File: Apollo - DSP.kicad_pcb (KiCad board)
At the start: 4 copper layers, 74.9 x 58 mm, 73 parts, among them J1 USB_C_Receptacle_USB2.0, J2 Conn_01x04, J3 MEM2067-02-180-00-A_REVB, J4 Conn_01x04, J5 Conn_01x04, J6 Conn_01x04, J7 Conn_01x06, U1 NCP115ASN330T2G, U2 USBLC6-2SC6, U3 NCP115ASN330T2G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

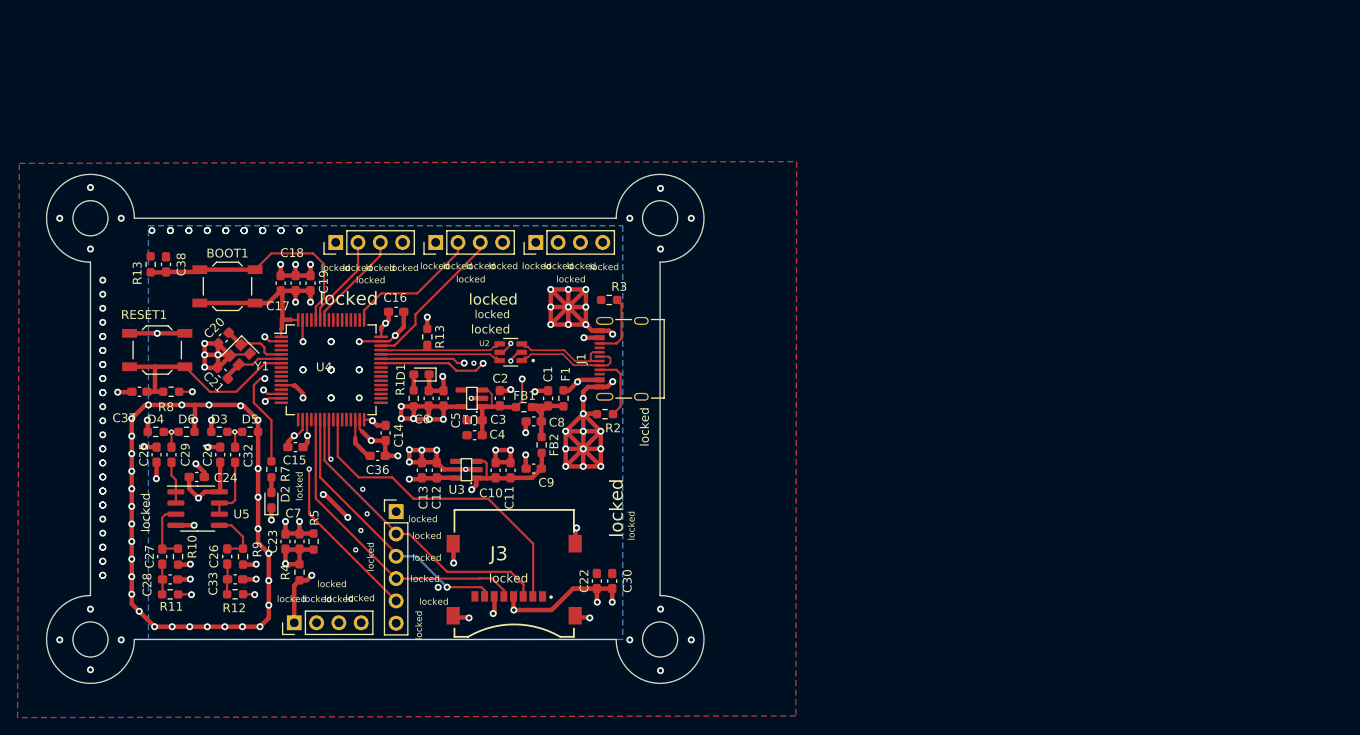
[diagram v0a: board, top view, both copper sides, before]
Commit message: fancy copper on edges
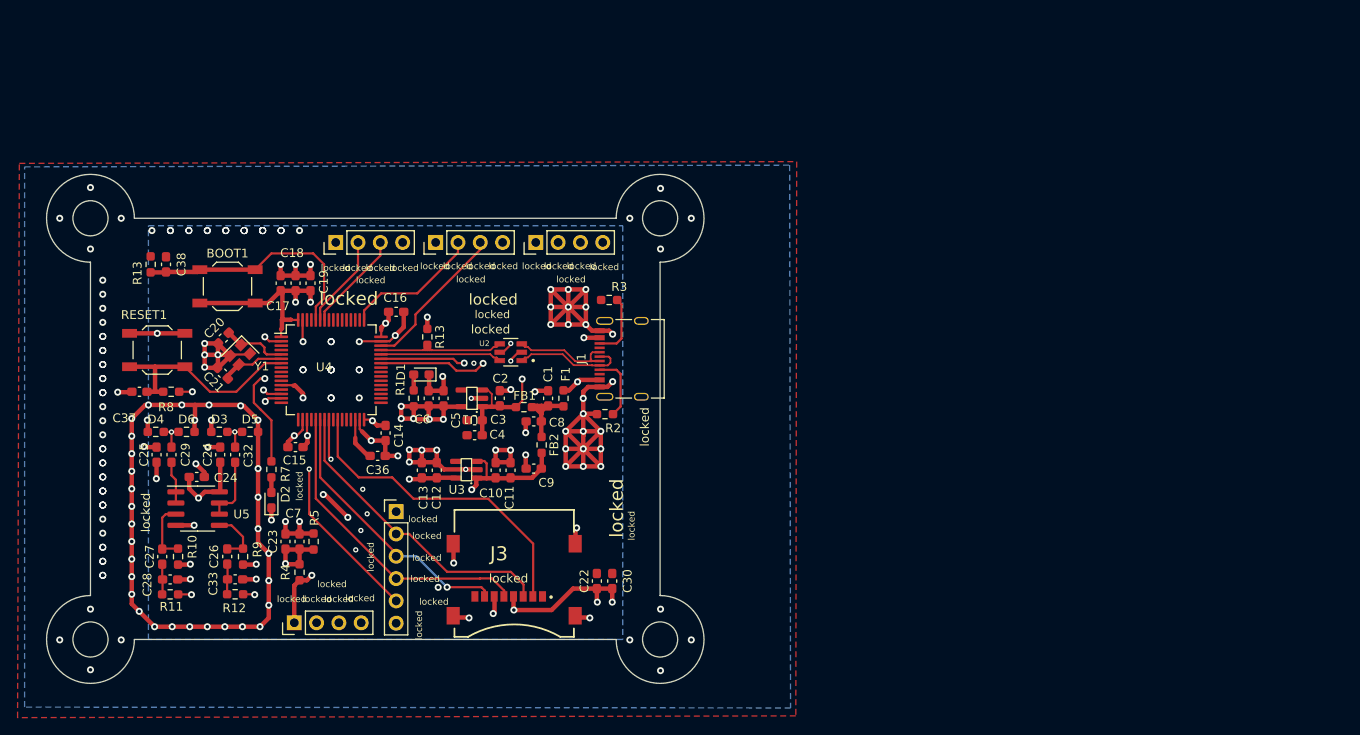
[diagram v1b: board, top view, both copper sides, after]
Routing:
- added copper zone on B.Cu, net GND
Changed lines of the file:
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@@
     )
   )
+  (gr_circle (center 54 77) (end 59 77)
+    (stroke (width 0.15) (type solid)) (fill solid) (layer "B.Mask"))
+  (gr_circle (center 54 125.1) (end 59 125.1)
+    (stroke (width 0.15) (type solid)) (fill solid) (layer "B.Mask"))
   (gr_circle (center 54 77.1) (end 59 77.1)
     (stroke (width 0.15) (type solid)) (fill solid) (layer "F.Mask"))
@@
     )
   )
-  (zone locked (net 2) (net_name "GND") (layer "In1.Cu") (hatch edge 0.508)
+  (zone locked (net 2) (net_name "GND") (layers "In1.Cu" "B.Cu") (hatch edge 0.508)
     (connect_pads (clearance 0.508))
     (min_thickness 0.254) (filled_areas_thickness no)
@@
     )
   )
-  (zone (net 0) (net_name "") (layer "F.Mask") (hatch edge 0.5)
+  (zone (net 0) (net_name "") (layers "*.Mask") (hatch edge 0.5)
     (connect_pads (clearance 0))
     (min_thickness 0.25) (filled_areas_thickness no)
@@
     )
   )
-  (zone (net 0) (net_name "") (layer "F.Mask") (hatch edge 0.5)
+  (zone (net 0) (net_name "") (layers "*.Mask") (hatch edge 0.5)
     (connect_pads (clearance 0))
     (min_thickness 0.25) (filled_areas_thickness no)
@@
     )
   )
-  (zone (net 0) (net_name "") (layer "F.Mask") (hatch edge 0.5)
+  (zone (net 0) (net_name "") (layers "*.Mask") (hatch edge 0.5)
     (connect_pads (clearance 0))
     (min_thickness 0.25) (filled_areas_thickness no)

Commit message: moved analog power farther away from digital Power, removed SPI and I2C Interface since it was not needed in the V1
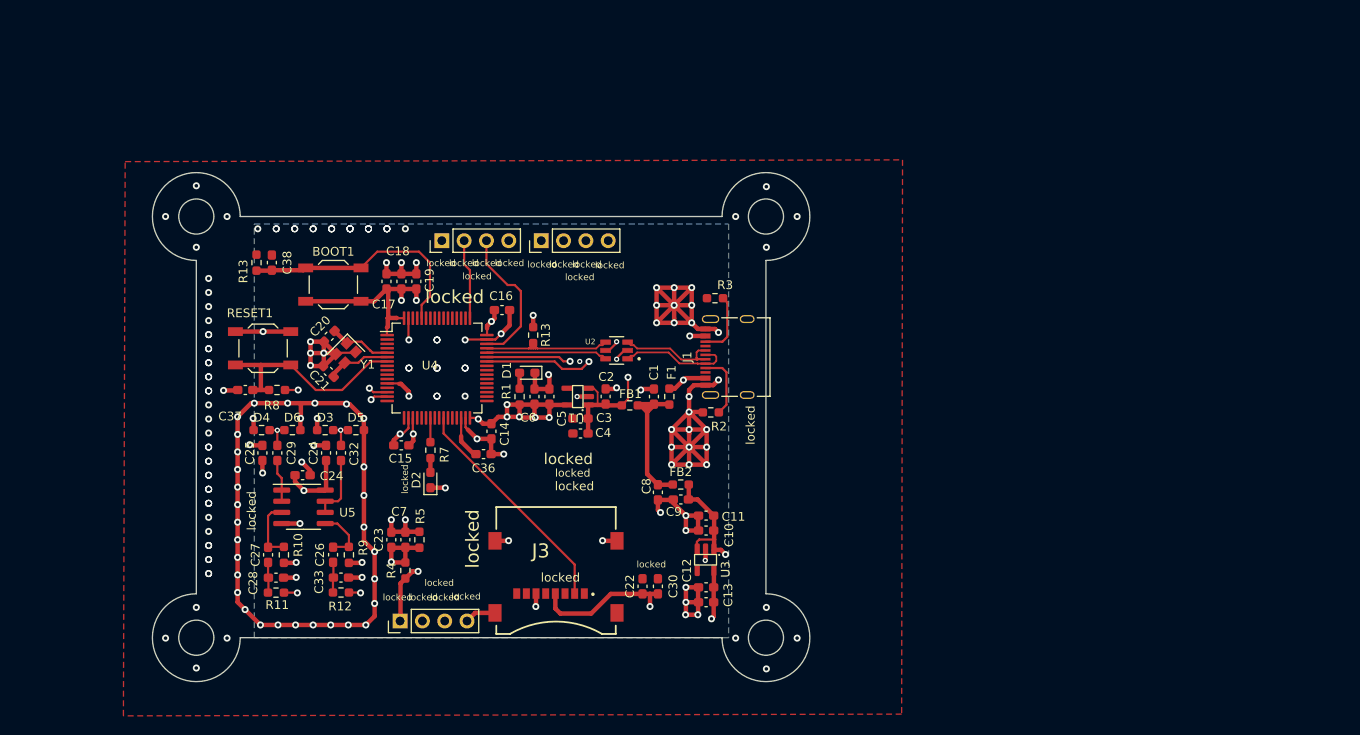
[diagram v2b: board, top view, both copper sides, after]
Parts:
- removed J4: Conn_01x04, Connector_PinHeader_2.54mm:PinHeader_1x04_P2.54mm_Vertical
- removed J7: Conn_01x06, Connector_PinHeader_2.54mm:PinHeader_1x06_P2.54mm_Vertical
- moved C13 35.7 mm to (124.1, 120.8), turned to 180 degrees
- moved C12 33.4 mm to (124.1, 119.1), turned to 180 degrees
- moved U3 29.1 mm to (124.0, 116.0), turned to -90 degrees
- moved C10 24.9 mm to (124.1, 112.7), turned to 180 degrees
- moved C11 22.9 mm to (124.1, 111.0), turned to 180 degrees
- moved D2 18.2 mm to (92.7, 106.9)
- moved R7 18.2 mm to (92.7, 103.5)
- moved C9 17.1 mm to (121.2, 109.1)
- moved FB2 16.5 mm to (121.2, 107.4), turned to 0 degrees
- moved C8 16.3 mm to (118.6, 108.3), turned to -90 degrees
- moved BOOT1 12.1 mm to (81.7, 84.7)
- moved C1 12.1 mm to (118.2, 97.4)
- moved C14 12.1 mm to (99.7, 101.3)
- moved C19 12.1 mm to (89.4, 84.3)
- moved C2 12.1 mm to (112.7, 97.4)
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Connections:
- R7 pad 1: Net-(U4-PC13) -> Net-(U4-PA7)
- U4 pad 2: Net-(U4-PC13) -> unconnected-(U4-PC13-Pad2)
- U4 pad 21: SCLK -> unconnected-(U4-PA5-Pad21)
- U4 pad 22: MISO -> unconnected-(U4-PA6-Pad22)
- U4 pad 23: MOSI -> Net-(U4-PA7)
- U4 pad 24: CONN_nCS -> unconnected-(U4-PC4-Pad24)
- U4 pad 58: SCL -> unconnected-(U4-PB6-Pad58)
- U4 pad 59: SDA -> unconnected-(U4-PB7-Pad59)
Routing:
- net SCLK: track 35.6 -> 0.00 mm
- net MOSI: track 35.0 -> 0.00 mm
- net MISO: track 31.7 -> 0.00 mm, vias 1 -> 0
- net CONN_nCS: track 26.7 -> 0.00 mm, vias 2 -> 0
- net +3.3VA: track 65.6 -> 91.0 mm
- net Net-(U4-PC13): track 17.9 -> 0.00 mm, vias 2 -> 0
- net +5VA: track 65.1 -> 80.0 mm, vias 5 -> 3
- net SCL: track 11.5 -> 0.00 mm
- net SDA: track 10.6 -> 0.00 mm
- net SD_nCS: track 36.8 -> 26.2 mm
- net VBUS: track 10.5 -> 20.4 mm
- net SWCLK: track 15.7 -> 9.10 mm
- net Tx: track 30.7 -> 26.2 mm
- net Rx: track 27.8 -> 23.7 mm
- net Net-(U4-PA7): track 0.00 -> 2.76 mm
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- removed copper zone on B.Cu, net GND

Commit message: cleaned up the whole board
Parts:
- removed the C24 at (80.8, 103.8)
- removed C25: 100n, Capacitor_SMD:C_0603_1608Metric_Pad1.08x0.95mm_HandSolder
- R4, R5: value 1k -> 5k1
- moved R13 36.9 mm to (106.1, 66.1), turned to -90 degrees
- moved C38 33.8 mm to (104.3, 66.1), turned to -90 degrees
- moved C8 31.7 mm to (139.2, 84.2), turned to 180 degrees
- moved C23 29.3 mm to (109.5, 93.5)
- moved C7 29.3 mm to (111.1, 93.5)
- moved R4 29.3 mm to (111.1, 97.0)
- moved R5 29.3 mm to (112.7, 93.5)
- moved C24 28.7 mm to (101.8, 90.1), turned to 0 degrees
- moved C10 28.5 mm to (144.8, 93.1)
- moved C11 28.5 mm to (144.8, 91.4)
- moved C12 28.5 mm to (144.8, 99.6)
- moved C13 28.5 mm to (144.8, 101.3)
- moved U3 28.5 mm to (144.8, 96.4)
- moved C9 28.2 mm to (138.4, 86.8), turned to 90 degrees
- moved FB2 28.0 mm to (140.1, 86.8), turned to -90 degrees
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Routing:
- net +5VA: track 80.0 -> 65.0 mm, vias 3 -> 2
- net VBUS: track 20.4 -> 7.59 mm
- net GND: track 289.1 -> 282.1 mm, vias 186 -> 254
- net +3.3VA: track 91.0 -> 84.7 mm
- net 3.3V: track 70.8 -> 75.7 mm, vias 13 -> 14
- net VAA: track 21.9 -> 25.0 mm
- net BOOT0: track 27.9 -> 25.3 mm
- net SWCLK: track 9.10 -> 9.85 mm
- net Tx: track 26.2 -> 27.0 mm
- net SWDIO: track 16.5 -> 17.3 mm
- net Rx: track 23.7 -> 24.5 mm
- added copper zone on B.Cu, net GND
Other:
- board text added: "BOOT"
- board text added: "RST"

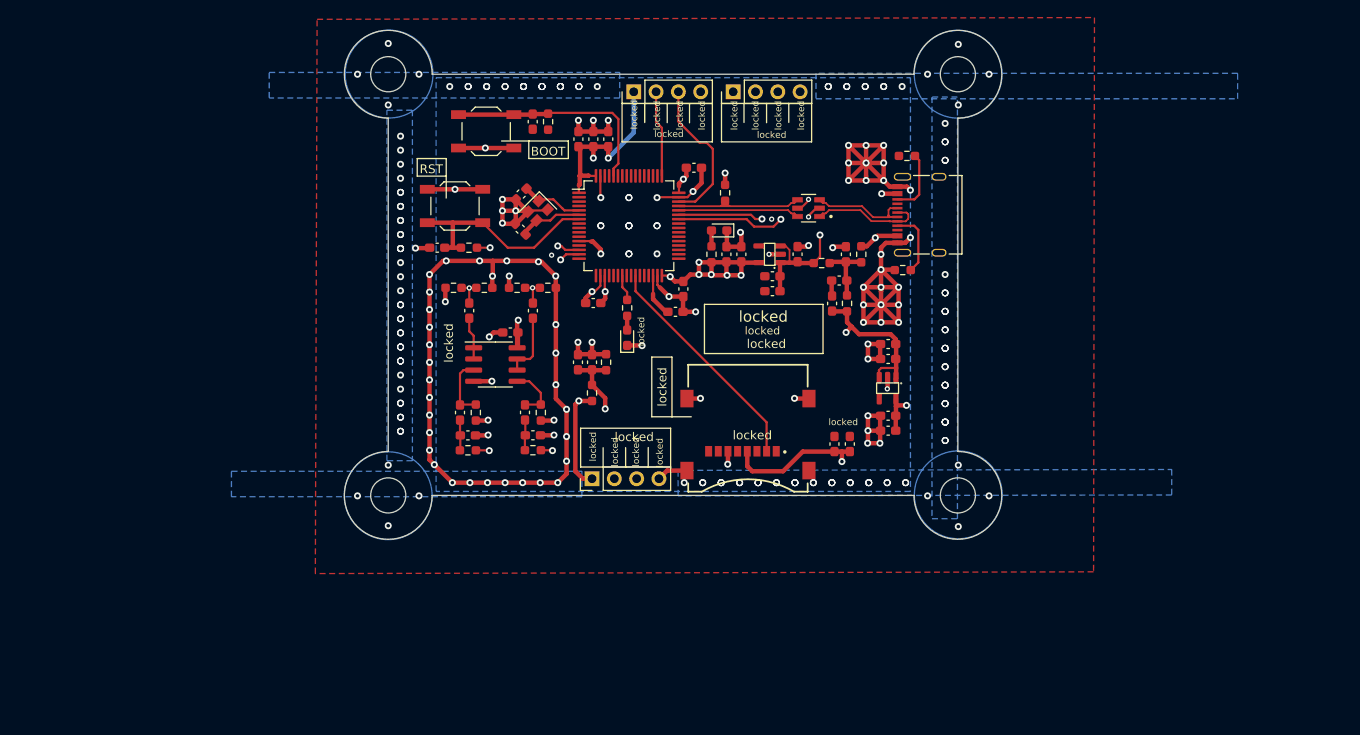
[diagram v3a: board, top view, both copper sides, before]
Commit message: made analog circuitry a bit more compact moved whole board
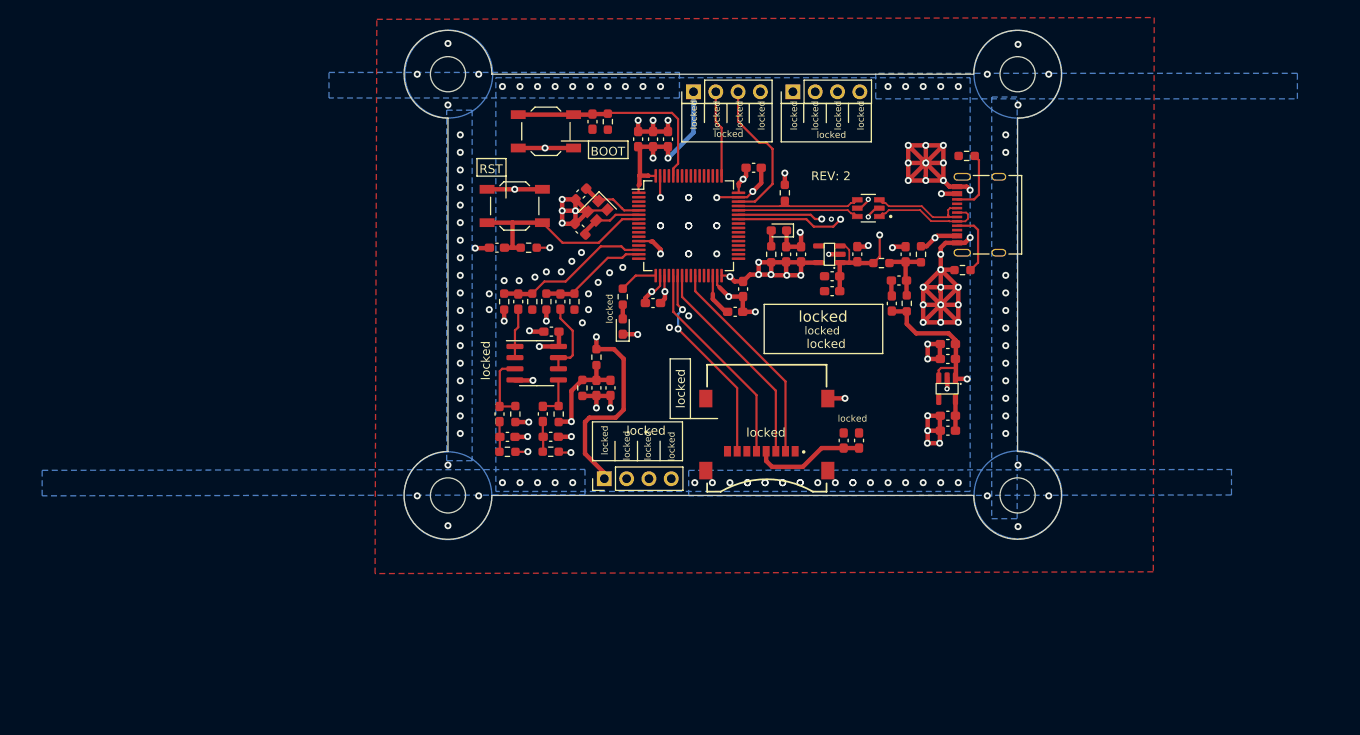
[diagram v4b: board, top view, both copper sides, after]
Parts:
- removed U5: LM358, Package_SO:SOIC-8_3.9x4.9mm_P1.27mm
- added U6: MCP602, Package_SO:SOIC-8_3.9x4.9mm_P1.27mm, F.Cu at (104.8, 93.6)
- moved C1 6.80 mm to (146.8, 81.2)
- moved C10 6.80 mm to (151.6, 93.1)
- moved C11 6.80 mm to (151.6, 91.4)
- moved C12 6.80 mm to (151.6, 99.6)
- moved C13 6.80 mm to (151.6, 101.3)
- moved C14 6.80 mm to (128.3, 85.2)
- moved C2 6.80 mm to (141.3, 81.2)
- moved C20 6.80 mm to (109.8, 74.3)
- moved C3 6.80 mm to (138.4, 83.7)
- moved C36 6.80 mm to (127.4, 87.8)
- moved C37 6.80 mm to (100.3, 80.5)
- moved C38 6.80 mm to (111.2, 66.1)
- moved C4 6.80 mm to (138.4, 85.4)
- moved C5 6.80 mm to (134.9, 81.2)
- moved F1 6.80 mm to (148.6, 81.2)
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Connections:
- J3 pad 5: SCLK -> SCK
- R7 pad 1: Net-(U4-PA7) -> Net-(U4-PA3)
- U4 pad 17: unconnected-(U4-PA3-Pad17) -> Net-(U4-PA3)
- U4 pad 21: unconnected-(U4-PA5-Pad21) -> SCK
- U4 pad 22: unconnected-(U4-PA6-Pad22) -> MISO
- U4 pad 23: Net-(U4-PA7) -> MOSI
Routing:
- net GND: track 282.1 -> 197.1 mm, vias 254 -> 176
- net +3.3VA: track 84.7 -> 40.6 mm, vias 4 -> 3
- net MOSI: track 0.00 -> 24.4 mm
- net SCK: track 0.00 -> 23.9 mm
- net MISO: track 0.00 -> 23.2 mm, vias 0 -> 2
- net +5VA: track 65.0 -> 72.4 mm
- net VAA: track 25.0 -> 18.2 mm, vias 3 -> 2
- net Net-(U4-PA3): track 0.00 -> 4.37 mm
- net CH0_IN: track 18.6 -> 14.5 mm
- net Net-(U4-PA7): track 2.99 -> 0.00 mm
- net 3.3V: track 75.7 -> 72.9 mm, vias 14 -> 13
- net ADC_CH1_IN: track 10.4 -> 12.6 mm, vias 2 -> 0
- net SD_nCS: track 26.2 -> 24.3 mm
- net CH1_IN: track 13.3 -> 11.6 mm
- net /Analog/CH1_+: track 6.39 -> 4.80 mm
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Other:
- board text added: "REV: 2"

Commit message: cleanup
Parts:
- moved C10 4.15 mm to (147.5, 93.2)
- moved C11 4.15 mm to (147.5, 91.5)
- moved C12 4.15 mm to (147.5, 99.6)
- moved C13 4.15 mm to (147.5, 101.3)
- moved U3 4.15 mm to (147.4, 96.5)
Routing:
- net +3.3VA: track 40.6 -> 79.8 mm, vias 3 -> 5
- net +5VA: track 72.4 -> 64.4 mm
- net 3.3V: track 72.9 -> 74.6 mm, vias 13 -> 14
- net GND: vias 176 -> 181

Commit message: finished?
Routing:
- net GND: track 197.1 -> 198.7 mm, vias 181 -> 182
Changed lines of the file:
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@@
   (segment locked (start 128.3 86.0125) (end 126.6625 86.0125) (width 0.508) (layer "F.Cu") (net 2))
   (segment (start 150.8 82.95) (end 152.3125 82.95) (width 0.508) (layer "F.Cu") (net 2))
+  (segment (start 128.725 103.625) (end 128.725 102.025) (width 0.508) (layer "F.Cu") (net 2))
   (segment locked (start 152.665 79.9) (end 153.55 79.9) (width 0.508) (layer "F.Cu") (net 2))
   (segment locked (start 107.703813 76.246187) (end 107.7 76.25) (width 0.508) (layer "F.Cu") (net 2))
@@
   (segment (start 150.8 86.95) (end 148.8 88.95) (width 0.508) (layer "F.Cu") (net 2))
   (segment (start 151.35 79.9) (end 150.8 80.45) (width 0.508) (layer "F.Cu") (net 2))
+  (segment (start 128.725 102.025) (end 128.7 102) (width 0.508) (layer "F.Cu") (net 2))
   (segment locked (start 110.496187 76.246187) (end 110.610051 76.360051) (width 0.254) (layer "F.Cu") (net 2))
   (segment locked (start 107.7 77.65) (end 107.7 76.25) (width 0.508) (layer "F.Cu") (net 2))
@@
   (via (at 114.9 62.1) (size 0.8) (drill 0.4) (layers "F.Cu" "B.Cu") (free) (net 2))
   (via locked (at 122.1 74.75) (size 0.8) (drill 0.4) (layers "F.Cu" "B.Cu") (net 2))
+  (via (at 128.7 102) (size 0.8) (drill 0.4) (layers "F.Cu" "B.Cu") (net 2))
   (via (at 99.4 85.7) (size 0.8) (drill 0.4) (layers "F.Cu" "B.Cu") (net 2))
   (via (at 152.8 62.1) (size 0.8) (drill 0.4) (layers "F.Cu" "B.Cu") (free) (net 2))
